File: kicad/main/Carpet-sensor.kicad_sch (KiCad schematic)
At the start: 22 parts, among them Q13 2N3906_C49023424, Q14 2N3904, Q15 2N3904, U4 RS8422XK

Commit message: Cliff/bumper connector reverse engineered
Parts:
- removed US1: WAFER-GH1_25-2PWB, JLCImport:WAFER-GH1_25-2PWB, symbol JLCImport:WAFER-GH1_25-2PWB
- added US1: S2B-ZR-SM4A-TF_LF_SN, JLCImport:S2B-ZR-SM4A-TF_LF_SN, symbol JLCImport:S2B-ZR-SM4A-TF_LF_SN
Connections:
- net ECHO: now also US1.1
- net GND: now also US1.0, US1.2
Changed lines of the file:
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@@
-	)
-	(junction
-		(at 316.23 147.955)
-		(diameter 0)
-		(color 0 0 0 0)
 	)
 	(junction
@@
 	(wire
 		(pts
-			(xy 319.405 147.955) (xy 316.23 147.955)
-		)
-		(stroke
-			(width 0)
-			(type default)
-		)
-	)
-	(wire
-		(pts
 			(xy 222.25 131.445) (xy 240.03 131.445)
 		)
@@
 	(wire
 		(pts
-			(xy 316.23 144.145) (xy 316.23 147.955)
-		)
-		(stroke
-			(width 0)
-			(type default)
-		)
-	)
-	(wire
-		(pts
 			(xy 279.4 238.76) (xy 307.34 238.76)
 		)
@@
 	(wire
 		(pts
-			(xy 316.23 128.905) (xy 319.405 128.905)
-		)
-		(stroke
-			(width 0)
-			(type default)
-		)
-	)
-	(wire
-		(pts
 			(xy 295.275 228.6) (xy 295.275 233.68)
 		)
@@
 	(wire
 		(pts
-			(xy 319.405 128.905) (xy 319.405 147.955)
-		)
-		(stroke
-			(width 0)
-			(type default)
-		)
-	)
-	(wire
-		(pts
 			(xy 318.77 231.14) (xy 318.77 254.635)
 		)
@@
 	(wire
 		(pts
-			(xy 304.8 147.955) (xy 316.23 147.955)
+			(xy 304.8 147.955) (xy 322.58 147.955)
 		)
 		(stroke
@@
 	(wire
 		(pts
+			(xy 322.58 139.065) (xy 318.77 139.065)
+		)
+		(stroke
+			(width 0)
+			(type default)
+		)
+	)
+	(wire
+		(pts
 			(xy 234.315 252.095) (xy 234.315 267.335)
 		)
@@
 	(wire
 		(pts
+			(xy 322.58 147.955) (xy 322.58 139.065)
+		)
+		(stroke
+			(width 0)
+			(type default)
+		)
+	)
+	(wire
+		(pts
 			(xy 304.8 136.525) (xy 308.61 136.525)
 		)
@@
 		(pts
 			(xy 234.315 236.22) (xy 256.54 236.22)
-		)
-		(stroke
-			(width 0)
-			(type default)
-		)
-	)
-	(wire
-		(pts
-			(xy 316.23 131.445) (xy 316.23 128.905)
 		)
 		(stroke
@@
 			)
 			(justify right)
-		)
-	)
-	(symbol
-		(lib_id "JLCImport:WAFER-GH1_25-2PWB")
-		(at 313.69 137.795 0)
-		(unit 1)
-		(body_style 1)
-		(exclude_from_sim no)
-		(in_bom yes)
-		(on_board yes)
-		(in_pos_files yes)
-		(dnp no)
-		(fields_autoplaced yes)
-		(property "Reference" "US1"
-			(at 320.675 136.5249 0)
-			(show_name no)
-			(do_not_autoplace no)
-			(effects
-				(font
-					(size 1.27 1.27)
-				)
-				(justify left)
-			)
-		)
-		(property "Value" "WAFER-GH1_25-2PWB"
-			(at 320.675 139.0649 0)
-			(show_name no)
-			(do_not_autoplace no)
-			(effects
-				(font
-					(size 1.27 1.27)
-				)
-				(justify left)
-			)
-		)
-		(property "Footprint" "JLCImport:WAFER-GH1_25-2PWB"
-			(at 313.69 137.795 0)
-			(hide yes)
-			(show_name no)
-			(do_not_autoplace no)
-			(effects
-				(font
-					(size 1.27 1.27)
-				)
-			)
-		)
-		(property "Datasheet" "https://wmsc.lcsc.com/wmsc/upload/file/pdf/v2/lcsc/2205271730_XUNPU-WAFER-GH1-25-2PWB_C3029377.pdf"
-			(at 313.69 137.795 0)
-			(hide yes)
-			(show_name no)
-			(do_not_autoplace no)
-			(effects
-				(font
-					(size 1.27 1.27)
-				)
-			)
-		)
-		(property "Description" "-25℃~+85℃ 1 1.25mm 125V 1A 1x2P 2 2P 4.35mm 5.75mm 5mm Auxiliary Solder Pin Beige Brass GH LCP Surface Mount, Right Angle Tin SMD,P=1.25mm,卧贴 Wire To Board Connector ROHS"
-			(at 313.69 137.795 0)
-			(hide yes)
-			(show_name no)
-			(do_not_autoplace no)
-			(effects
-				(font
-					(size 1.27 1.27)
-				)
-			)
-		)
-		(property "LCSC" "C3029377"
-			(at 313.69 137.795 0)
-			(hide yes)
-			(show_name no)
-			(do_not_autoplace no)
-			(effects
-				(font
-					(size 1.27 1.27)
-				)
-			)
-		)
-		(property "Manufacturer" "XUNPU"
-			(at 313.69 137.795 0)
-			(hide yes)
-			(show_name no)
-			(do_not_autoplace no)
-			(effects
-				(font
-					(size 1.27 1.27)
-				)
-			)
-		)
-		(property "Manufacturer Part" "WAFER-GH1.25-2PWB"
-			(at 313.69 137.795 0)
-			(hide yes)
-			(show_name no)
-			(do_not_autoplace no)
-			(effects
-				(font
-					(size 1.27 1.27)
-				)
-			)
-		)
-		(pin "1"
-		)
-		(pin "3"
-		)
-		(pin "2"
-		)
-		(pin "4"
-		)
-		(instances
-			(project "Main"
-				(path "/dbcfb655-8d45-4808-9a74-2a0eb03372e8/b8feb78a-8098-4bc8-81b4-34551e1a6113"
-					(reference "US1")
-					(unit 1)
-				)
-			)
 		)
 	)
@@
 					(unit 1)
 				)
+			)
+		)
+	)
+	(symbol
+		(lib_id "JLCImport:S2B-ZR-SM4A-TF_LF_SN")
+		(at 311.15 139.065 0)
+		(unit 1)
+		(body_style 1)
+		(exclude_from_sim no)
+		(in_bom yes)
+		(on_board yes)
+		(in_pos_files yes)
+		(dnp no)
+		(fields_autoplaced yes)
+		(property "Reference" "US1"
+			(at 313.69 129.54 0)
+			(show_name no)
+			(do_not_autoplace no)
+			(effects
+				(font
+					(size 1.27 1.27)
+				)
+			)
+		)
+		(property "Value" "S2B-ZR-SM4A-TF_LF_SN"
+			(at 313.69 132.08 0)
+			(show_name no)
+			(do_not_autoplace no)
+			(effects
+				(font
+					(size 1.27 1.27)
+				)
+			)
+		)
+		(property "Footprint" "JLCImport:S2B-ZR-SM4A-TF_LF_SN"
+			(at 311.15 139.065 0)
+			(hide yes)
+			(show_name no)
+			(do_not_autoplace no)
+			(effects
+				(font
+					(size 1.27 1.27)
+				)
+			)
+		)
+		(property "Datasheet" "https://www.lcsc.com/datasheet/lcsc_datasheet_1912111437_JST-S2B-ZR-SM4A-TF-LF-SN_C265329.pdf"
+			(at 311.15 139.065 0)
+			(hide yes)
+			(show_name no)
+			(do_not_autoplace no)
+			(effects
+				(font
+					(size 1.27 1.27)
+				)
+			)
+		)
+		(property "Description" "-25℃~+85℃ 1 1.5mm 1A 1x2P 2 2P 3.7mm 50V 6.5mm 6mm Auxiliary Solder Pin Brass PA6T Surface Mount, Right Angle Tin UL94V-0 White ZH SMD,P=1.5mm,卧贴 Wire To Board Connector ROHS"
+			(at 311.15 139.065 0)
+			(hide yes)
+			(show_name no)
+			(do_not_autoplace no)
+			(effects
+				(font
+					(size 1.27 1.27)
+				)
+			)
+		)
+		(property "LCSC" "C265329"
+			(at 311.15 139.065 0)
+			(hide yes)
+			(show_name no)
+			(do_not_autoplace no)
+			(effects
+				(font
+					(size 1.27 1.27)
+				)
+			)
+		)
+		(property "Manufacturer" "JST"
+			(at 311.15 139.065 0)
+			(hide yes)
+			(show_name no)
+			(do_not_autoplace no)
+			(effects
+				(font
+					(size 1.27 1.27)
+				)
+			)
+		)
+		(property "Manufacturer Part" "S2B-ZR-SM4A-TF(LF)(SN)"
+			(at 311.15 139.065 0)
+			(hide yes)
+			(show_name no)
+			(do_not_autoplace no)
+			(effects
+				(font
+					(size 1.27 1.27)
+				)
+			)
+		)
+		(pin "1"
+		)
+		(pin "0"
+		)
+		(pin "2"
+		)
+		(instances
+			(project "Main"
+				(path "/dbcfb655-8d45-4808-9a74-2a0eb03372e8/b8feb78a-8098-4bc8-81b4-34551e1a6113"
+					(reference "US1")
+					(unit 1)
+				)

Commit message: STM32 power rail switch
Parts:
- C18, C21, C22: value 100nF/50V -> 100nF/25V; LCSC C1591 -> C1590
- R24, R26, R33, R46: LCSC (none) -> C2907005
- R56, R63, R69, R70: LCSC (none) -> C2907088
- R67: LCSC (none) -> C98220
- R68, R71: LCSC (none) -> C2907113
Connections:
- net VCC-3V3-P renamed VCC-3V3-REG

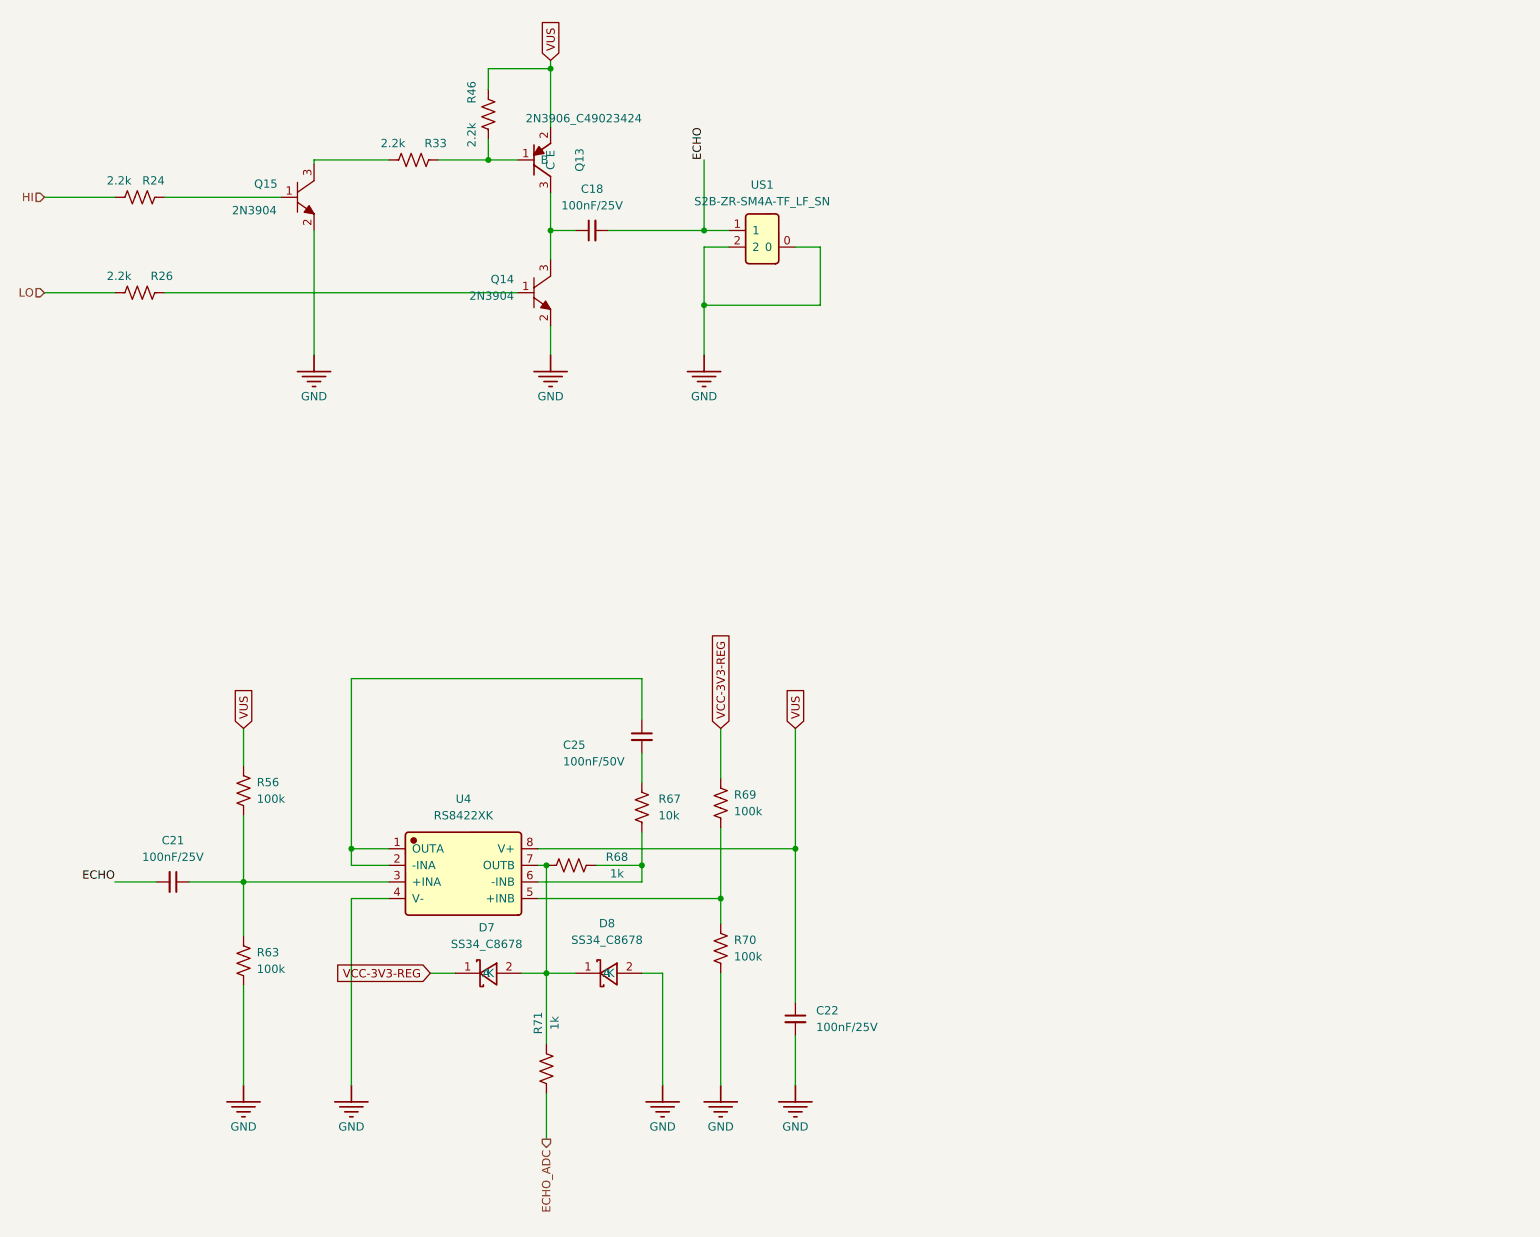
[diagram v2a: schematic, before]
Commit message: Update Power Control sch, Charger sch, Speaker + Mic, JTAG and Watch Dog
**Power Control:** Replaced the BJT with a MOSFET. The MCU hang condition is not covered yet.
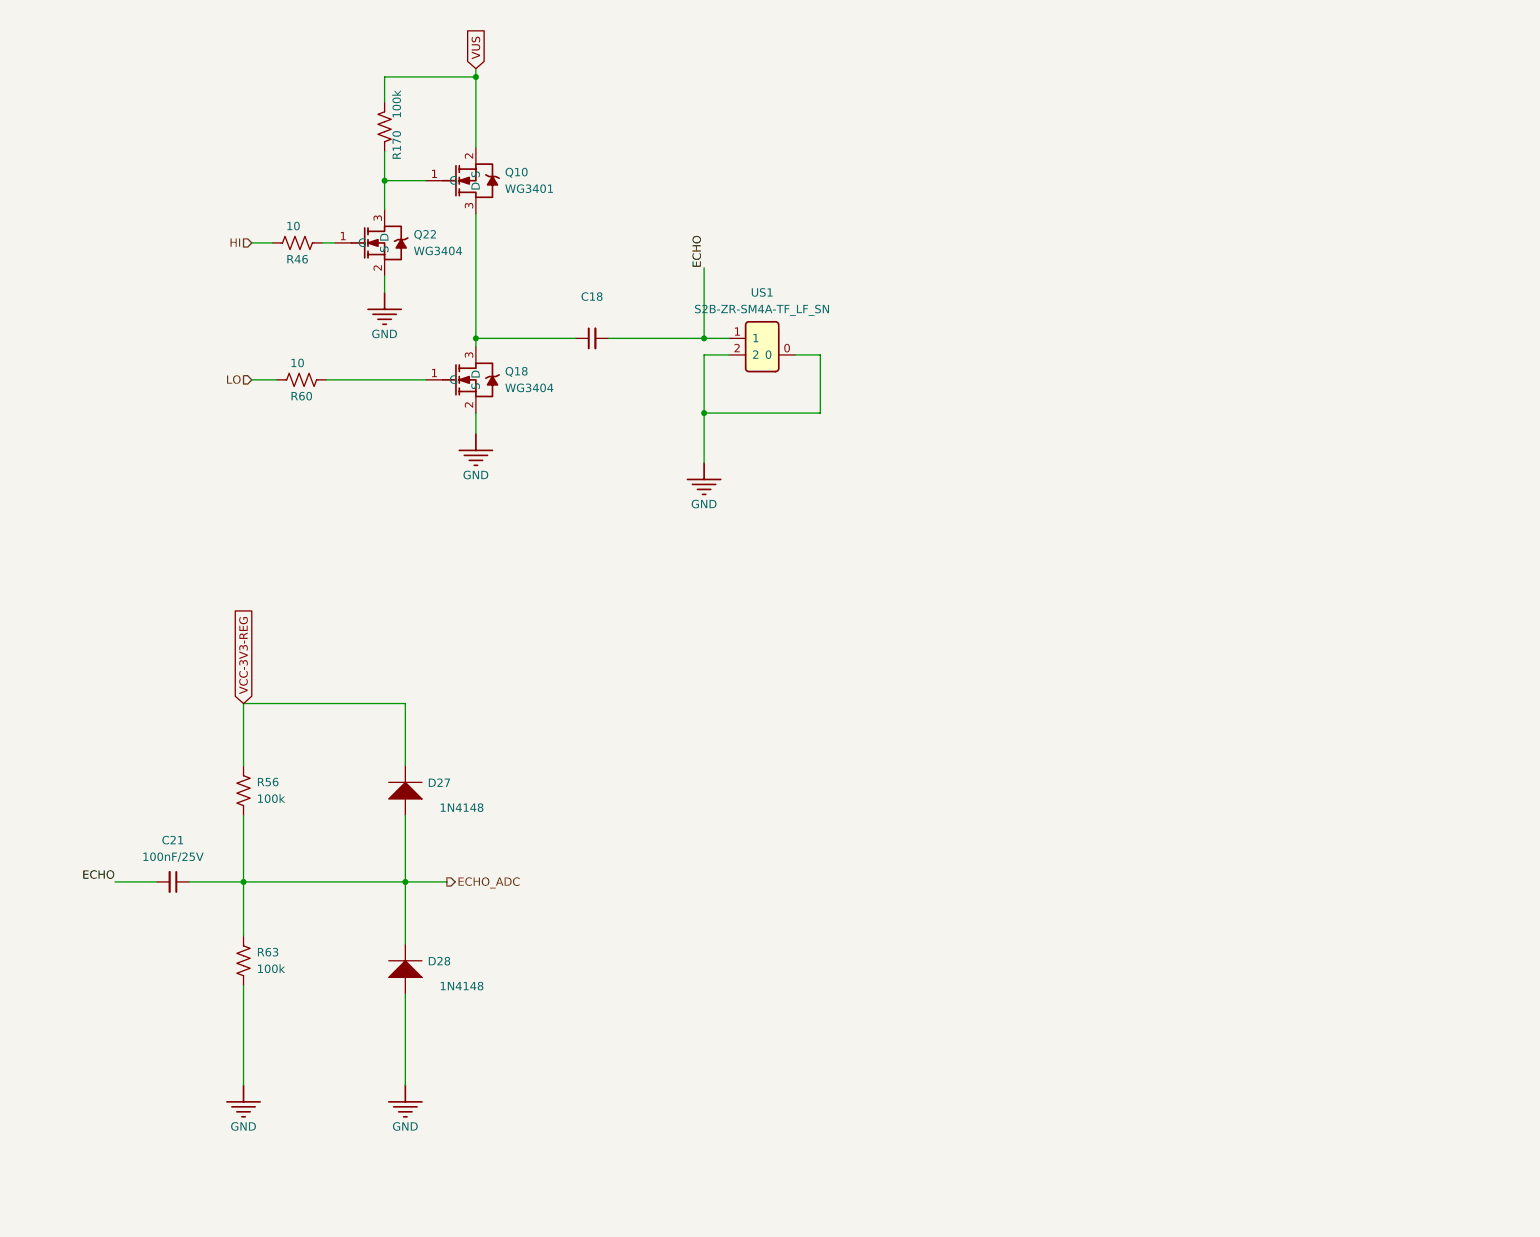
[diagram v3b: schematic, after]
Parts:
- removed C22: 100nF/25V, Capacitor_SMD:C_0603_1608Metric, symbol Device:C_Small
- removed C25: 100nF/50V, Capacitor_SMD:C_0603_1608Metric, symbol Device:C_Small
- removed D7, D8: SS34_C8678, JLCImport:SS34_C8678, symbol JLCImport:SS34_C8678
- removed Q13: 2N3906_C49023424, JLCImport:2N3906_C49023424, symbol JLCImport:2N3906_C49023424
- removed Q14, Q15: 2N3904, oomwoo_altium:SOT23-3D, symbol DesignLibrary:POWER_0_mirrored_NPN-SOT23_DesignLibrary.SchLib
- removed R24, R26, R33: 2.2k, Resistor_SMD:R_0603_1608Metric, symbol Device:R_US
- removed R67: 10k, Resistor_SMD:R_0603_1608Metric, symbol Device:R_US
- removed R68, R71: 1k, Resistor_SMD:R_0603_1608Metric, symbol Device:R_US
- removed R69, R70: 100k, Resistor_SMD:R_0603_1608Metric, symbol Device:R_US
- removed U4: RS8422XK, JLCImport:RS8422XK, symbol JLCImport:RS8422XK
- added D27, D28: 1N4148, oomwoo_altium:SOD123, symbol DesignLibrary:POWER_2_DIODE-1_DesignLibrary.SchLib
- added Q10: WG3401, JLCImport:WG3401, symbol JLCImport:WG3401
- added Q18, Q22: WG3404, JLCImport:WG3404, symbol JLCImport:WG3404
- added R170: 100k, Resistor_SMD:R_0603_1608Metric, symbol Device:R_US
- added R60: 10, Resistor_SMD:R_0603_1608Metric, symbol Device:R_US
- R46: value 2.2k -> 10; LCSC C2907005 -> C2907091
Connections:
- net ECHO_ADC: now also C21.1, R56.2, R63.1, D27.1 (A), D28.2 (K)
- net GND: now also D28.1 (A), Q18.2 (S), Q22.2 (S)
- net HI: now also R46.2
- net LO: now also R60.2
- net VCC-3V3-REG: now also R56.1, D27.2 (K)
- net VUS: now also Q10.2 (S), R170.2; no longer R46.2, R56.1
- net at R46.1: now also Q22.1 (G)
- net at C18.1: now also Q10.3 (D), Q18.3 (D)
- new net: Q10.1 (G), Q22.3 (D), R170.1
- new net: Q18.1 (G), R60.1
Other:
- moved on the sheet: C18, US1

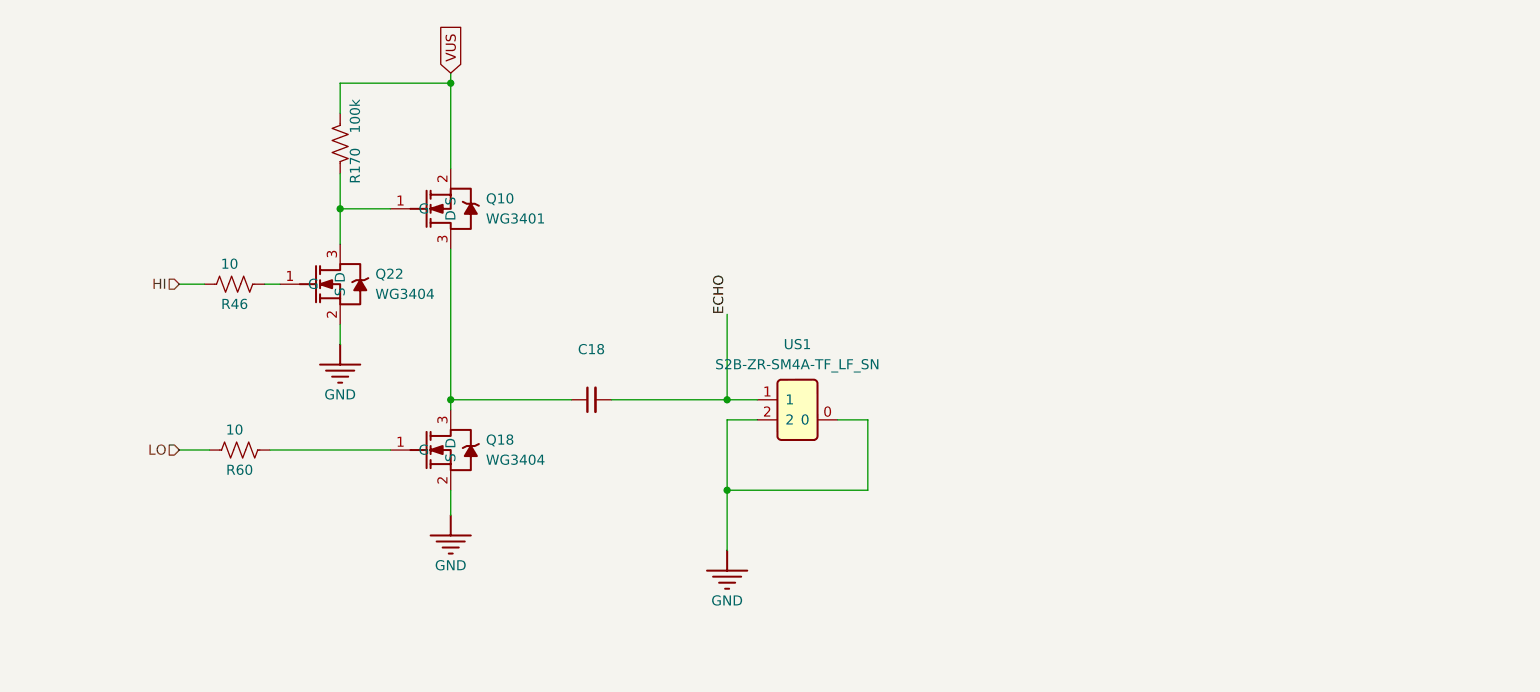
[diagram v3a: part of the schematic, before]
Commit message: Replaced slow P-FET with resistor
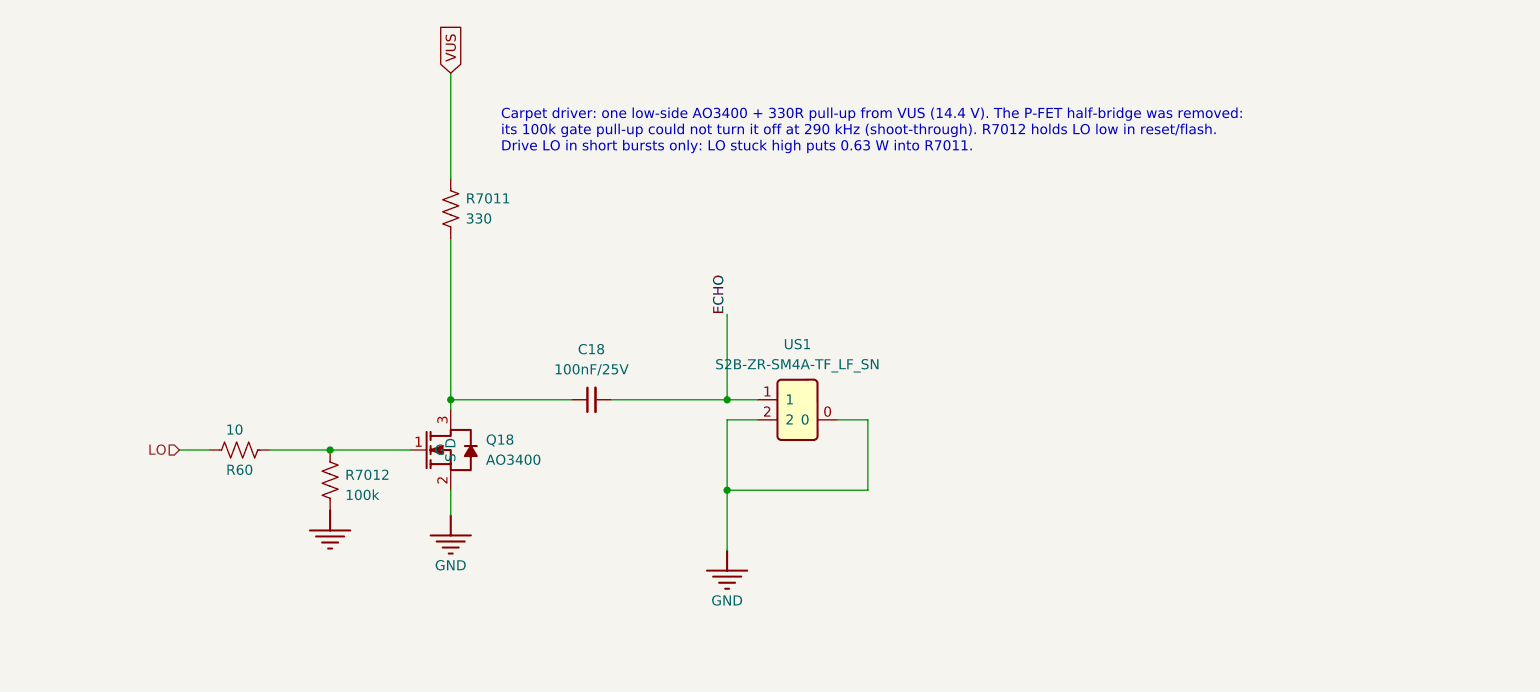
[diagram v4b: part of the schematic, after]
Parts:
- removed Q10: WG3401, JLCImport:WG3401, symbol JLCImport:WG3401
- removed Q22: WG3404, JLCImport:WG3404, symbol JLCImport:WG3404
- removed R170: 100k, Resistor_SMD:R_0603_1608Metric, symbol Device:R_US
- removed R46: 10, Resistor_SMD:R_0603_1608Metric, symbol Device:R_US
- added R7011: 330, Resistor_SMD:R_1206_3216Metric, symbol Device:R_US
- added R7012: 100k, Resistor_SMD:R_0603_1608Metric, symbol Device:R_US
- Q18: value WG3404 -> AO3400; footprint JLCImport:WG3404 -> JLCImport:AO3400; symbol JLCImport:WG3404 -> JLCImport:AO3400; LCSC C7541480 -> C20628874; Manufacturer Wild Goose -> FOSAN; Manufacturer Part WG3404 -> AO3400
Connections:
- net GND: now also R7012.2
- net VUS: now also R7011.1
- net at Q18.1 (G), R60.1: now also R7012.1
- net at C18.1, Q18.3 (D): now also R7011.2
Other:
- note added: "Carpet driver: one low-side AO3400 + 330R pull-up from VUS (14.4 V). The P-FET half-bridge was removed: its 100k gate pull-up could not turn it off at 290 kHz (shoot-through). R7012 holds LO low in reset/flash. Drive LO in short bursts only: LO stuck high puts 0.63 W into R7011."
